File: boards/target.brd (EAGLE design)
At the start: 25.4 x 25.4 mm, 20 parts, among them Q1 BC847BS, U1 MCP1703T-3002E/CB, X1 53398-04, X2 53398-04

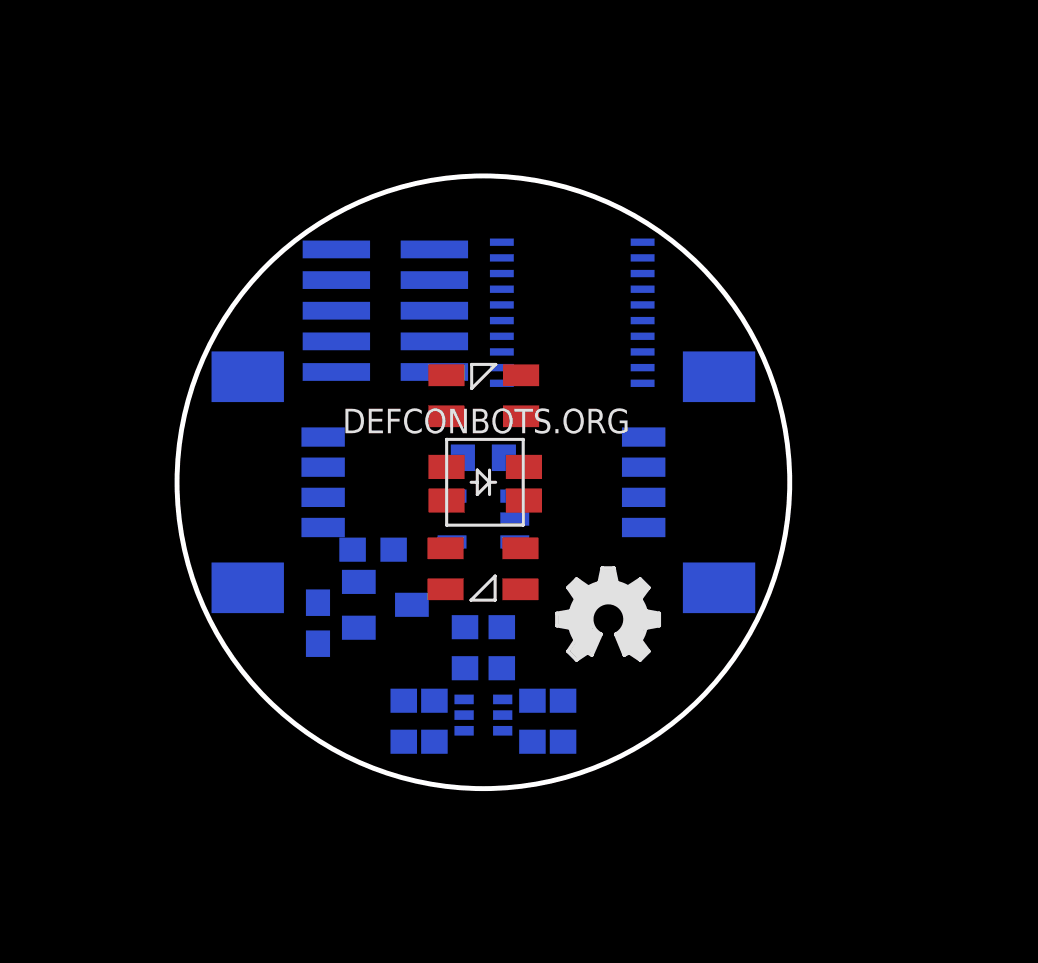
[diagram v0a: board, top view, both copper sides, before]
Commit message: Rename to target.sch/brd. Fix controller. Add part numbers. Still needs to be routed.
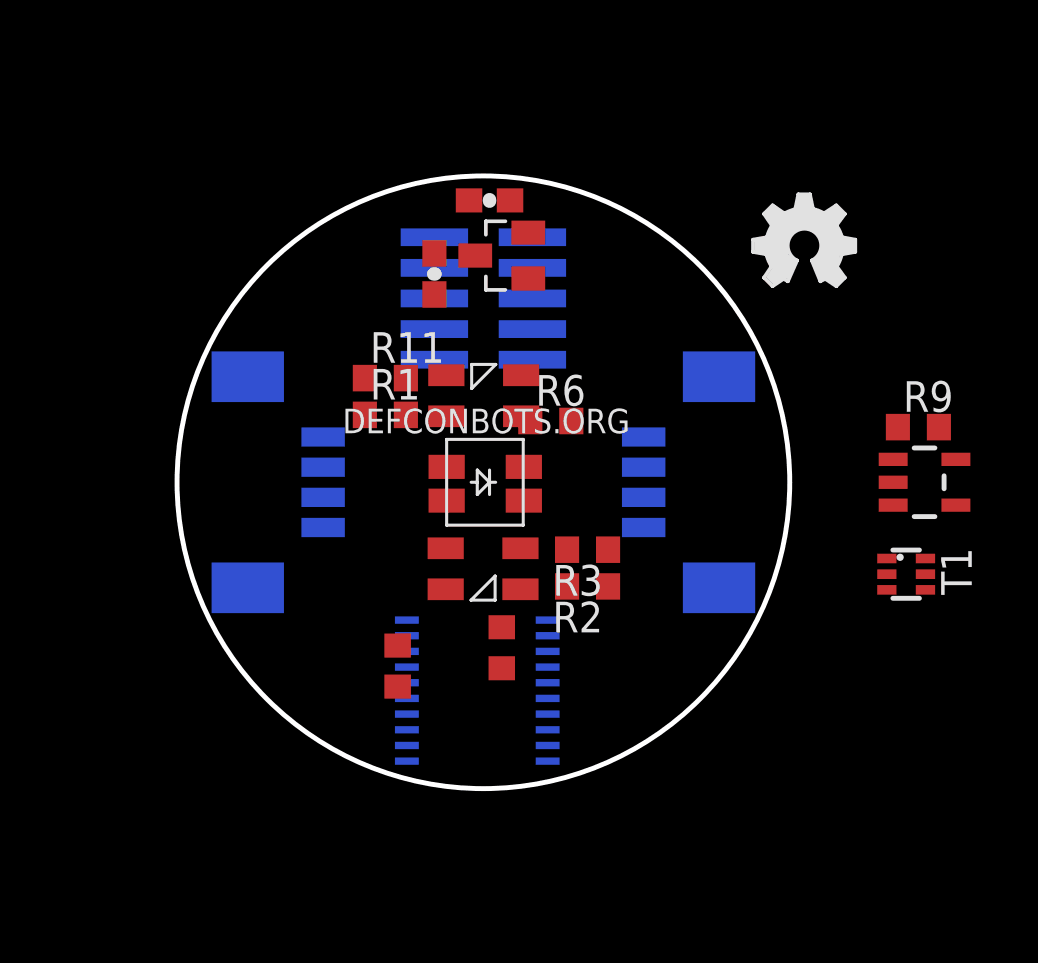
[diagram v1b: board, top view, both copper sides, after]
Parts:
- removed LPC812: LPC812M101JDH20, LPC800:TSSOP20
- removed Q1: BC847BS, transistor-small-signal:SOT363_PHILIPS
- removed U$2: MCP6291T-E/OT, SparkFun-AnalogIC:SOT23-5
- removed U$3: FTSH-105, torpedo:FTSH-105-01-XXX-DV-K
- added JP2: FTSH-105-01-L, torpedo:FTSH-105-01-XXX-DV-K
- added R6: 71-CRCW0603-10K-E3, rcl:R0603
- added T1: 771-BC847BS-T/R, transistor-small-signal:SOT363_PHILIPS
- added U2: 771-LPC824M201JDH20J, torpedo:TSSOP20
- added U4: 579-MCP6291T-E/OT, SparkFun-AnalogIC:SOT23-5
- D3: value CLS15CLS15 -> 638-CLS1522CL213GTR8
- JP1, X1: value 53398-04 -> 798-DF134P125V20
- R1, R3: value CRCW0603200RFKEA -> 71-CRCW0603-5.6-E3
- R11, R2: value CRCW0603200RFKEA -> 71-CRCW060368R0FKEB
- R5, R8: value CRCW0603200RFKEA -> 71-CRCW0603220RFKEB
- R9: value CRCW0603200RFKEA -> 71-CRCW06034M64FKEA
- U1: value MCP1703T-3002E/CB -> 579-MCP1703T-3002ECB
- moved R9 18.1 mm to (30.7, 15.0), flipped to the top
- moved LOGO2 17.5 mm to (23.9, 20.8)
- moved C2 15.3 mm to (13.0, 24.4), flipped to the top
- moved C1 15.3 mm to (10.7, 21.3), flipped to the top
- moved U1 15.3 mm to (13.5, 22.1), flipped to the top
- moved R1 14.7 mm to (8.64, 15.5), flipped to the top, turned to 0 degrees
- moved R11 14.4 mm to (8.64, 17.0), flipped to the top, turned to 0 degrees
- moved R2 9.45 mm to (17.0, 8.38), flipped to the top, turned to 180 degrees
- moved R3 7.47 mm to (17.0, 9.91), flipped to the top, turned to 180 degrees
- moved R5 2.90 mm to (9.14, 5.08), flipped to the top, turned to 270 degrees
- flipped R8 to the top
- renumbered U$1 to D3, U$4 to D1, U$5 to D2, X2 to JP1
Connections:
- net +3V3: now also JP2.1, R6.1, U2.15, U4.5; no longer LPC812.15, U$2.5, U$3.1
- net BLUE_LED: now also U2.11; no longer LPC812.1
- net GND: now also JP2.3, JP2.5, JP2.9, T1.1, T1.4, U2.16, U4.2, U4.3; no longer LPC812.16, Q1.1, Q1.4, U$2.2, U$2.3, U$3.3, U$3.5, U$3.9
- net LASER_RX: now also U2.10, U4.1; no longer LPC812.3, U$2.1
- net N$1: now also T1.6; no longer Q1.6
- net N$11: now also T1.5; no longer Q1.5
- net N$2: now also T1.3; no longer Q1.3
- net N$4: now also T1.2; no longer Q1.2
- net N$5: now also U4.4; no longer U$2.4
- net RED_LED: now also U2.12; no longer LPC812.10
- net RST: now also JP2.10, R6.2, U2.5; no longer LPC812.4, U$3.10
- net RX: now also U2.3; no longer LPC812.8
- net SWCLK: now also JP2.4, U2.7; no longer LPC812.6, U$3.4
- net SWDIO: now also JP2.2, U2.8; no longer LPC812.7, U$3.2
- net TX: now also U2.2; no longer LPC812.9

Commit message: Working on target layout
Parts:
- moved LOGO2 23.2 mm to (3.05, 10.7)
- moved C2 22.1 mm to (9.91, 2.54), flipped to the bottom, turned to 0 degrees
- moved JP1 18.0 mm to (3.81, 12.7), turned to 270 degrees
- moved X1 18.0 mm to (21.6, 12.7), turned to 90 degrees
- moved U1 17.1 mm to (9.91, 5.33), flipped to the bottom, turned to 0 degrees
- moved U4 16.5 mm to (15.0, 8.64), flipped to the bottom, turned to 0 degrees
- moved C1 16.1 mm to (7.37, 5.59), flipped to the bottom
- moved U2 16.1 mm to (16.8, 19.6), turned to 90 degrees
- moved T1 14.9 mm to (16.3, 3.81), flipped to the bottom, turned to 0 degrees
- moved R9 14.7 mm to (16.3, 12.7), flipped to the bottom, turned to 90 degrees
- moved R2 12.0 mm to (8.64, 17.0), turned to 0 degrees
- moved R11 11.9 mm to (17.0, 8.64), turned to 180 degrees
- moved R3 10.1 mm to (8.64, 15.5), turned to 0 degrees
- moved R1 9.94 mm to (17.0, 10.2), turned to 180 degrees
- moved R5 9.20 mm to (18.3, 4.06), flipped to the bottom, turned to 90 degrees
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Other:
- board text removed: "DEFCONBOTS.ORG"

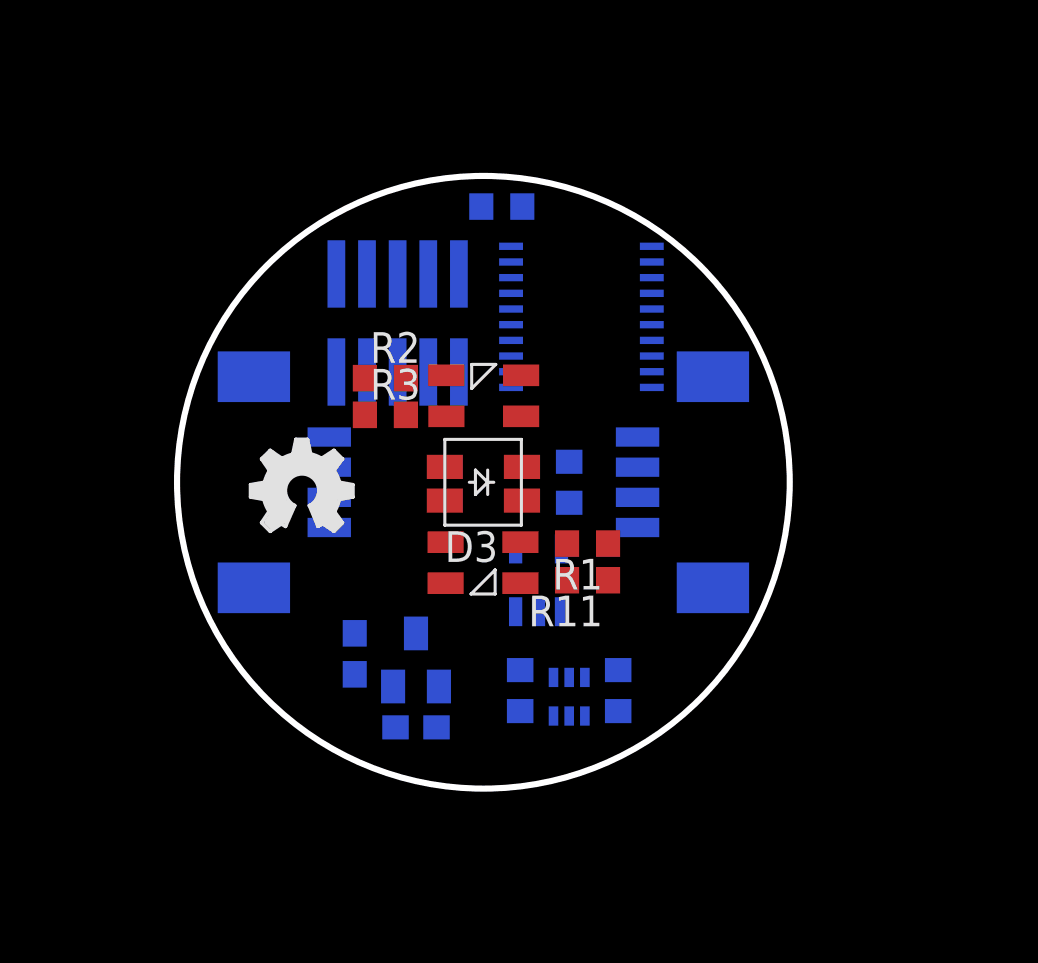
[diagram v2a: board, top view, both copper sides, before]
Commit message: First pass target route
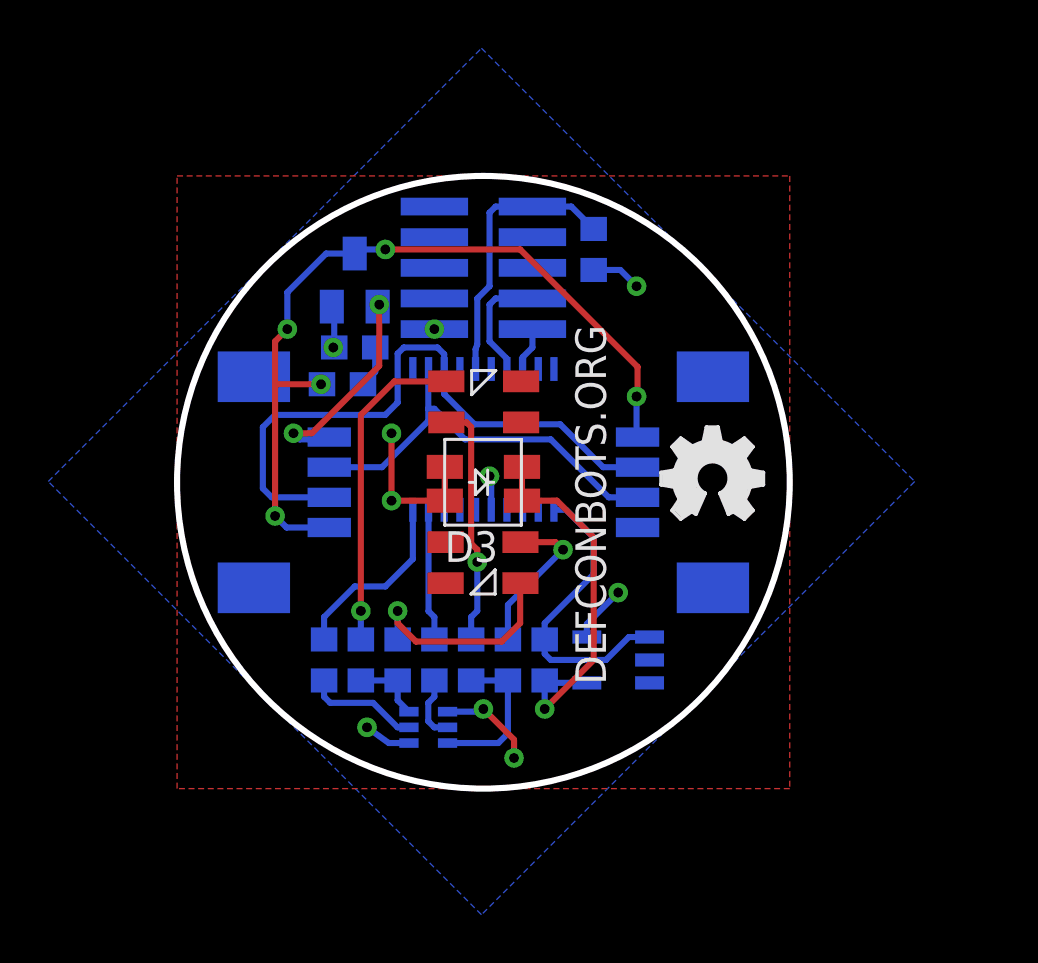
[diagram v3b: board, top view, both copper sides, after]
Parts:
- moved LOGO2 17.0 mm to (20.1, 11.2)
- moved C2 16.0 mm to (7.37, 18.3), turned to 180 degrees
- moved U1 16.0 mm to (7.37, 21.1)
- moved R5 12.3 mm to (6.10, 5.33)
- moved R2 11.7 mm to (7.62, 5.33), flipped to the bottom, turned to 90 degrees
- moved C1 11.2 mm to (6.86, 16.8), turned to 180 degrees
- moved R3 10.8 mm to (12.2, 5.33), flipped to the bottom, turned to 90 degrees
- moved R11 8.54 mm to (9.14, 5.33), flipped to the bottom, turned to 90 degrees
- moved R9 7.44 mm to (15.2, 5.33), turned to 270 degrees
- moved U2 6.51 mm to (12.7, 14.5), turned to 180 degrees
- moved T1 5.98 mm to (10.4, 2.54), turned to 90 degrees
- moved R1 5.85 mm to (13.7, 5.33), flipped to the bottom, turned to 90 degrees
- moved U4 4.67 mm to (18.3, 5.33), turned to 270 degrees
- moved JP2 4.23 mm to (12.7, 21.6), turned to 90 degrees
- moved R6 4.20 mm to (17.3, 22.4), turned to 90 degrees
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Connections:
- net BLUE_LED: now also U2.20; no longer U2.11
- net LASER_RX: now also U2.11; no longer U2.10
- net RED_LED: now also U2.19; no longer U2.12
- net RX: now also U2.2; no longer U2.3
- net TX: now also U2.3; no longer U2.2
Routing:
- net VIN: track 0.00 -> 34.3 mm, vias 0 -> 5
- net TX: track 0.00 -> 26.6 mm
- net GND: track 0.00 -> 23.2 mm, vias 0 -> 7
- net RX: track 0.00 -> 17.3 mm
- net N$5: track 0.00 -> 15.9 mm, vias 0 -> 1
- net N$6: track 0.00 -> 13.4 mm, vias 0 -> 1
- net LASER_RX: track 0.00 -> 12.6 mm
- net RST: track 0.00 -> 11.5 mm
- net N$8: track 0.00 -> 10.1 mm, vias 0 -> 1
- net N$3: track 0.00 -> 9.07 mm, vias 0 -> 1
- net BLUE_LED: track 0.00 -> 7.64 mm
- net +3V3: track 0.00 -> 7.64 mm, vias 0 -> 5
- net N$7: track 0.00 -> 6.56 mm, vias 0 -> 1
- net N$1: track 0.00 -> 6.39 mm
- net RED_LED: track 0.00 -> 5.48 mm
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- added copper zone on layer 1, net +3V3
- added copper zone on layer 16, net GND
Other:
- board text added: "DEFCONBOTS.ORG"
